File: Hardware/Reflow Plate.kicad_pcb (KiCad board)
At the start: 2 copper layers, 99.1 x 99.1 mm, 39 parts, among them J1 Barrel_Jack_MountingPin, J2 31-M-12, J3 Conn_02x03_Odd_Even, J4 Conn_02x03_Odd_Even, J5 Conn_02x03_Odd_Even, J6 Conn_02x03_Odd_Even, J7 Conn_01x04_Pin, Q2 Q_NMOS_GDS, U1 HUSB238, U3 STM32F103CBTx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

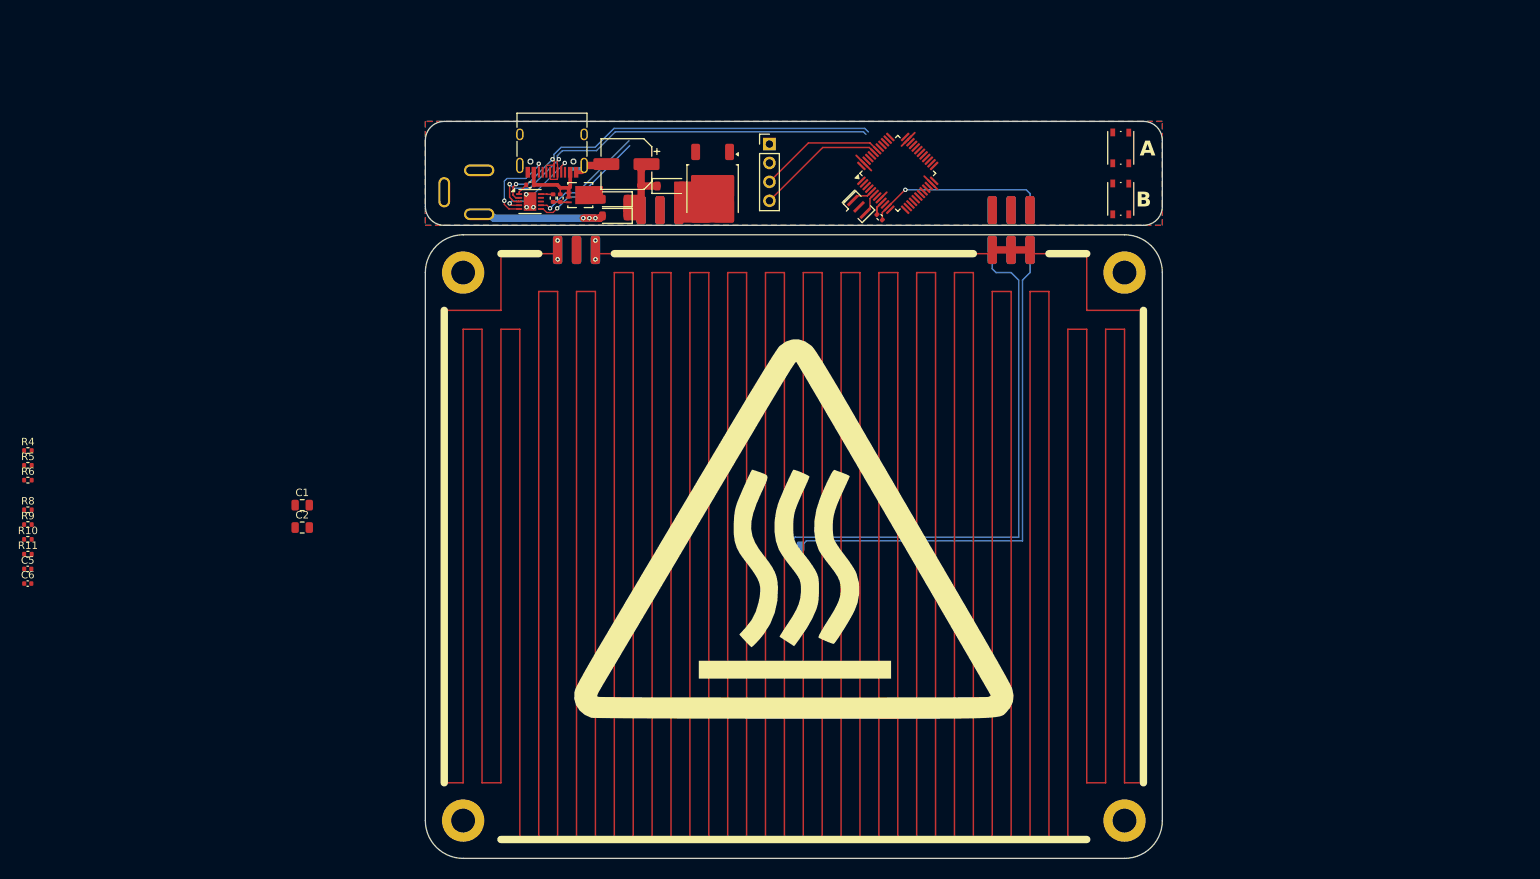
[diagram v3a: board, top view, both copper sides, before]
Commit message: Ditch rev 1, moving on to rev 2.
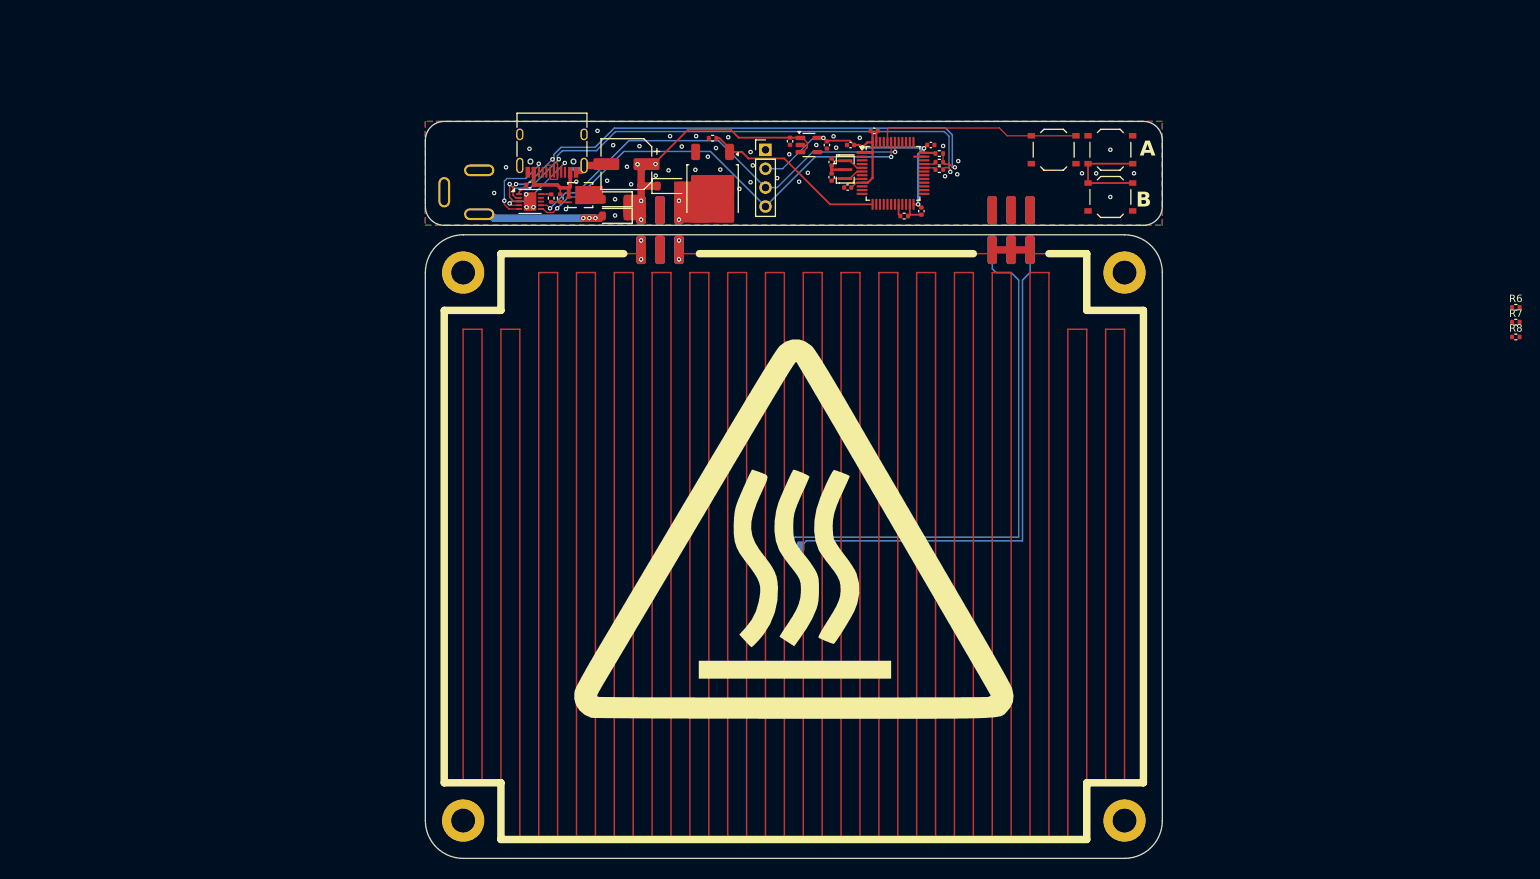
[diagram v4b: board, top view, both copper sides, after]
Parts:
- removed the REF** at (183.6, 39.1)
- removed the REF** at (183.6, 46.0)
- added C10: 100n, Capacitor_SMD:C_0402_1005Metric, F.Cu at (147.3, 38.7)
- added C11: 100n, Capacitor_SMD:C_0402_1005Metric, F.Cu at (150.5, 36.8)
- added C7: 100n, Capacitor_SMD:C_0402_1005Metric, F.Cu at (146.9, 44.5)
- added C8: 100n, Capacitor_SMD:C_0402_1005Metric, F.Cu at (156.8, 47.6)
- added C9: 100n, Capacitor_SMD:C_0402_1005Metric, F.Cu at (158.1, 38.7)
- added SW2: SW_Push, Button_Switch_SMD:SW_Push_1P1T_XKB_TS-1187A, F.Cu at (174.6, 39.4)
- added SW3: SW_Push, Button_Switch_SMD:SW_Push_1P1T_XKB_TS-1187A, F.Cu at (182.2, 39.4)
- added SW4: SW_Push, Button_Switch_SMD:SW_Push_1P1T_XKB_TS-1187A, F.Cu at (182.2, 45.7)
- added U2: TLV73333PDBV, Package_TO_SOT_SMD:SOT-23-5, F.Cu at (141.7, 38.7)
- C1, C2: value 22u -> 1u; footprint Capacitor_SMD:C_0805_2012Metric -> Capacitor_SMD:C_0402_1005Metric
- moved R6 201.3 mm to (236.7, 60.6)
- moved R8 201.3 mm to (236.7, 64.5)
- moved R11 133.8 mm to (159.3, 39.9), turned to 180 degrees
- moved R10 132.6 mm to (159.3, 41.0)
- moved R9 131.5 mm to (159.3, 42.0)
- moved R5 122.5 mm to (154.5, 48.3), turned to 180 degrees
- moved C5 121.1 mm to (144.8, 41.0), turned to 90 degrees
- moved C6 121.1 mm to (144.8, 43.1), turned to -90 degrees
- moved R4 101.2 mm to (128.8, 37.8), turned to 180 degrees
- moved C2 87.3 mm to (144.1, 38.7), turned to -90 degrees
- moved R7 86.7 mm to (236.7, 62.5), turned to 0 degrees
- moved C1 81.8 mm to (139.2, 38.2), turned to -90 degrees
- moved J7 18.3 mm to (135.9, 39.4)
- moved J3 11.2 mm to (121.7, 52.8)
- moved Y1 5.33 mm to (146.6, 42.0), turned to -90 degrees
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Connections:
- J2 pad A6: UDB_D+ -> USB_D+
- J2 pad A7: UDB_D- -> USB_D-
- J2 pad B6: UDB_D+ -> USB_D+
- J2 pad B7: UDB_D- -> USB_D-
- U1 pad 2: UDB_D+ -> USB_D+
- U1 pad 3: UDB_D- -> USB_D-
- U3 pad 1: unconnected-(U3-VBAT-Pad1) -> +3V3
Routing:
- net USB_D-: track 0.00 -> 77.7 mm, vias 0 -> 3
- net USB_D+: track 0.00 -> 77.6 mm, vias 0 -> 3
- net +3V3: track 2.01 -> 64.7 mm, vias 0 -> 4
- net UDB_D-: track 60.1 -> 0.00 mm, vias 2 -> 0
- net UDB_D+: track 58.5 -> 0.00 mm, vias 2 -> 0
- net +24V: track 12.9 -> 41.3 mm, vias 0 -> 4
- net BOOT0: track 0.00 -> 27.6 mm
- net SDA1: track 33.3 -> 58.5 mm, vias 1 -> 2
- net Heater_CTRL: track 0.00 -> 25.0 mm
- net SCL1: track 32.8 -> 57.4 mm, vias 1 -> 2
- net NTC_Measure: track 24.6 -> 0.00 mm, vias 1 -> 0
- net /Heater: track 2941.4 -> 2962.5 mm
- net GND: track 16.1 -> 18.9 mm, vias 3 -> 47
- net Net-(U3-PB2): track 0.00 -> 1.68 mm
- net Net-(U3-PA12): track 0.00 -> 1.65 mm
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
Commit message: Rev 'b'. Having this produced. Added some voltage monitors. cleaned up traces. Moved i2c lines to i2c2. forgot to add pull-ups. the ones in the display should work though.
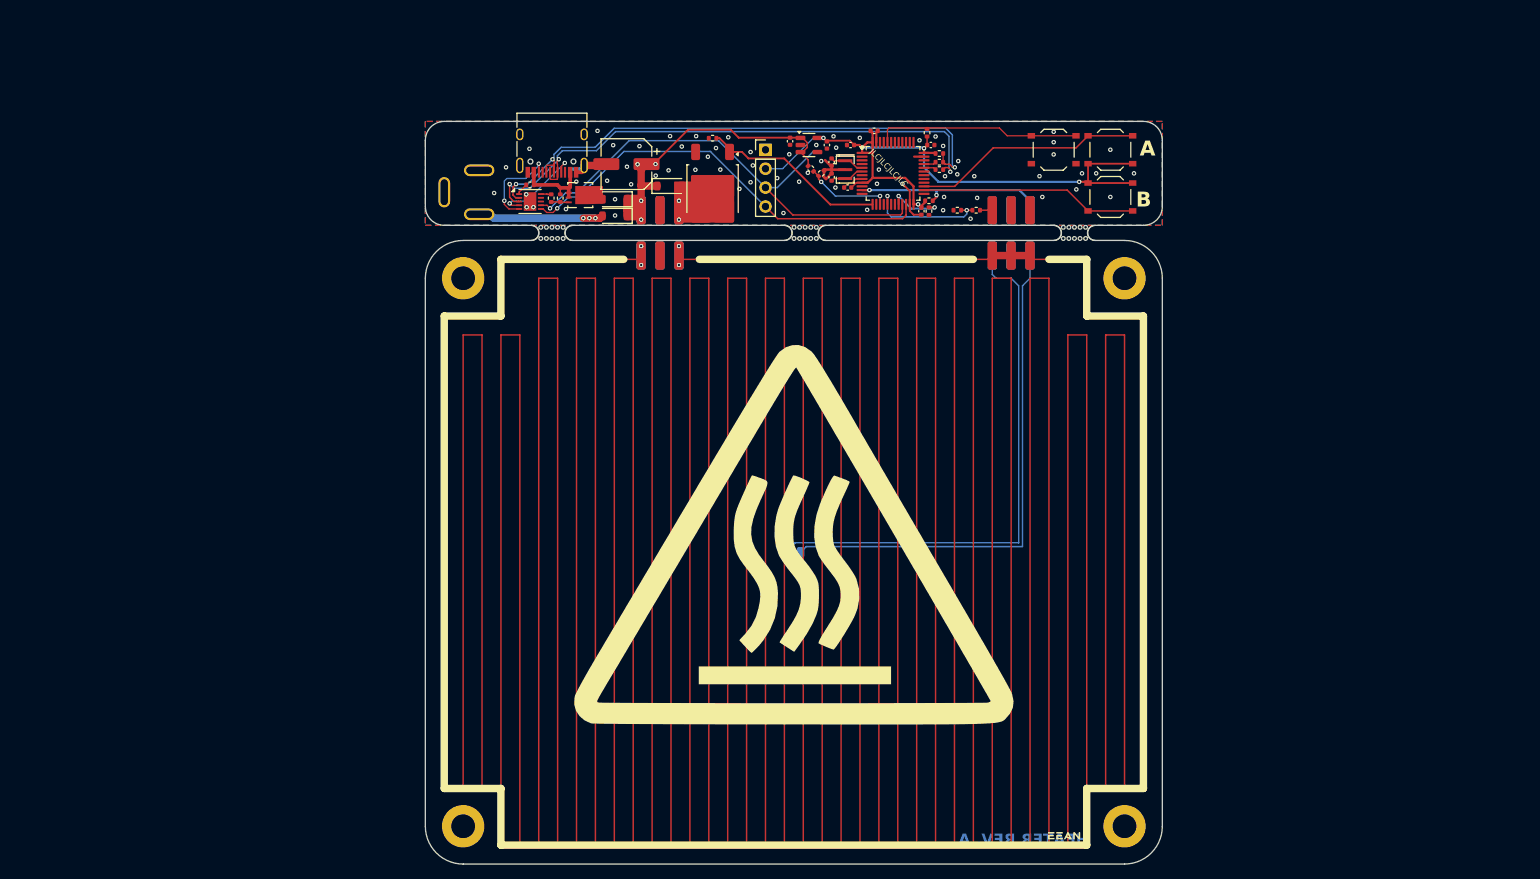
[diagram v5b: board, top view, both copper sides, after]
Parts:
- removed R8: 10k, Resistor_SMD:R_0402_1005Metric
- added G***: LOGO, EEAN_Customs:EEAN Logo 1.0, F.Cu at (176.0, 131.6)
- added R12: 100k, Resistor_SMD:R_0402_1005Metric, F.Cu at (142.0, 41.9)
- added R13: 11k, Resistor_SMD:R_0402_1005Metric, F.Cu at (143.4, 42.5)
- added R14: 100k, Resistor_SMD:R_0402_1005Metric, F.Cu at (164.2, 47.5)
- added R15: 11k, Resistor_SMD:R_0402_1005Metric, F.Cu at (161.7, 47.5)
- added mouse-bite-2mm-slot: VAL**, Panelization:mouse-bite-2mm-slot, F.Cu at (177.4, 50.5)
- added mouse-bite-2mm-slot: VAL**, Panelization:mouse-bite-2mm-slot, F.Cu at (141.2, 50.5)
- added mouse-bite-2mm-slot: VAL**, Panelization:mouse-bite-2mm-slot, F.Cu at (107.2, 50.5)
- moved R6 82.5 mm to (157.6, 37.1), turned to 90 degrees
- moved R7 80.6 mm to (157.9, 46.2)
- moved R5 3.39 mm to (157.9, 47.6), turned to 90 degrees
- moved G*** 0.76 mm to (139.7, 90.9)
- moved J3 0.76 mm to (121.7, 53.6)
- moved J4 0.76 mm to (168.9, 53.6)
- moved REF** 0.76 mm to (95.2, 130.3)
- moved REF** 0.76 mm to (95.2, 56.6)
- moved REF** 0.76 mm to (184.2, 56.6)
- moved REF** 0.76 mm to (184.2, 130.3)
- moved TH1 0.76 mm to (139.7, 93.5)
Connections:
- net +24V renamed VBUS
- net Net-(J6-Pin_1) renamed /HeatMon
- SW3 pad 2: unconnected-(SW3-Pad2) -> BTN_A
- SW4 pad 2: unconnected-(SW4-Pad2) -> BTN_B
- U3 pad 15: unconnected-(U3-PA5-Pad15) -> VCCMeasure
- U3 pad 17: unconnected-(U3-PA7-Pad17) -> HeaterMeasure
- U3 pad 21: unconnected-(U3-PB10-Pad21) -> SCL1
- U3 pad 22: unconnected-(U3-PB11-Pad22) -> SDA1
- U3 pad 26: unconnected-(U3-PB13-Pad26) -> BTN_B
- U3 pad 27: unconnected-(U3-PB14-Pad27) -> BTN_A
- U3 pad 42: SCL1 -> unconnected-(U3-PB6-Pad42)
- U3 pad 43: SDA1 -> unconnected-(U3-PB7-Pad43)
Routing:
- net BTN_A: track 0.00 -> 30.9 mm
- net BTN_B: track 0.00 -> 29.2 mm
- net +3V3: track 64.7 -> 93.0 mm, vias 4 -> 5
- net NTC_Measure: track 0.00 -> 26.1 mm, vias 0 -> 2
- net HeaterMeasure: track 0.00 -> 16.5 mm, vias 0 -> 2
- net VCCMeasure: track 0.00 -> 11.7 mm, vias 0 -> 2
- net SCL1: track 57.4 -> 66.3 mm, vias 2 -> 1
- net GND: track 18.9 -> 26.1 mm, vias 47 -> 67
- net Net-(U3-PB2): track 1.68 -> 7.48 mm, vias 0 -> 2
- net VBUS: track 41.3 -> 43.6 mm
- net /HeatMon: track 0.00 -> 1.65 mm
- net SDA1: track 58.5 -> 58.1 mm, vias 2 -> 1
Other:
- board size 99.1 x 99.1 mm -> 99.1 x 99.8 mm
- board text added: "100k NTC THERMISTOR"
- board text added: "HEATER REV. A"
- board text added: "JLCJLCJLCJLC"

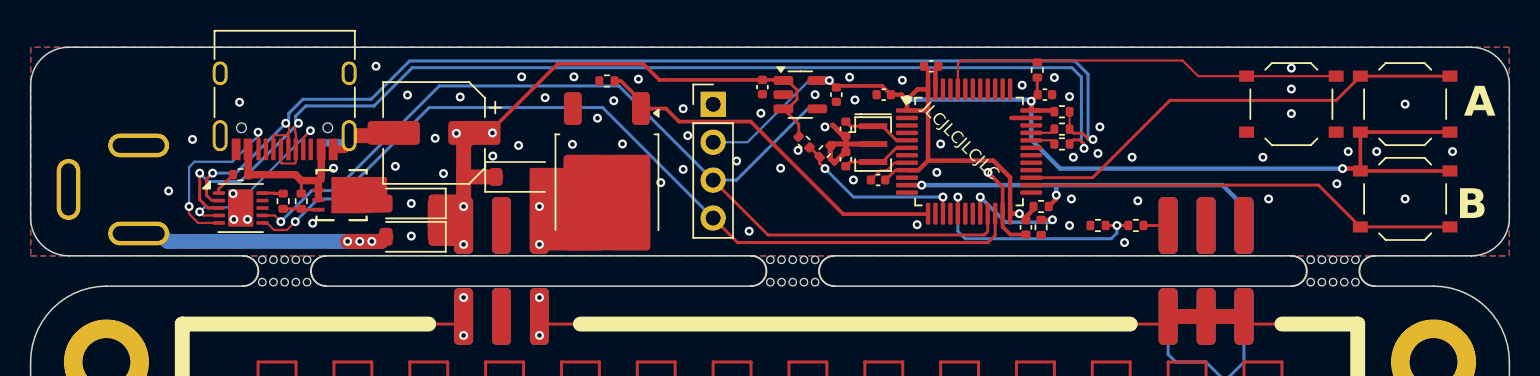
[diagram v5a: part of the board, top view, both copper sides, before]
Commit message: Initial Prototype gerbers. Found problems.
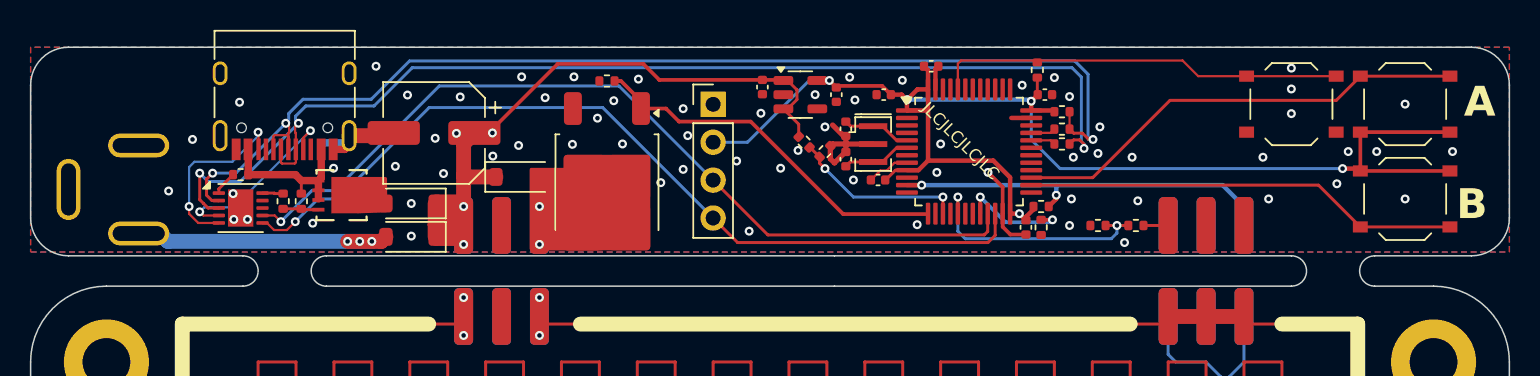
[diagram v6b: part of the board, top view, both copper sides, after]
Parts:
- removed mouse-bite-2mm-slot (x3): VAL**, Panelization:mouse-bite-2mm-slot
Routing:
- net SCL1: track 66.3 -> 57.9 mm
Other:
- outline, holes or cut-outs redrawn
- board text added: "${REFERENCE}"
